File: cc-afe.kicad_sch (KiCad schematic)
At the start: 10 parts

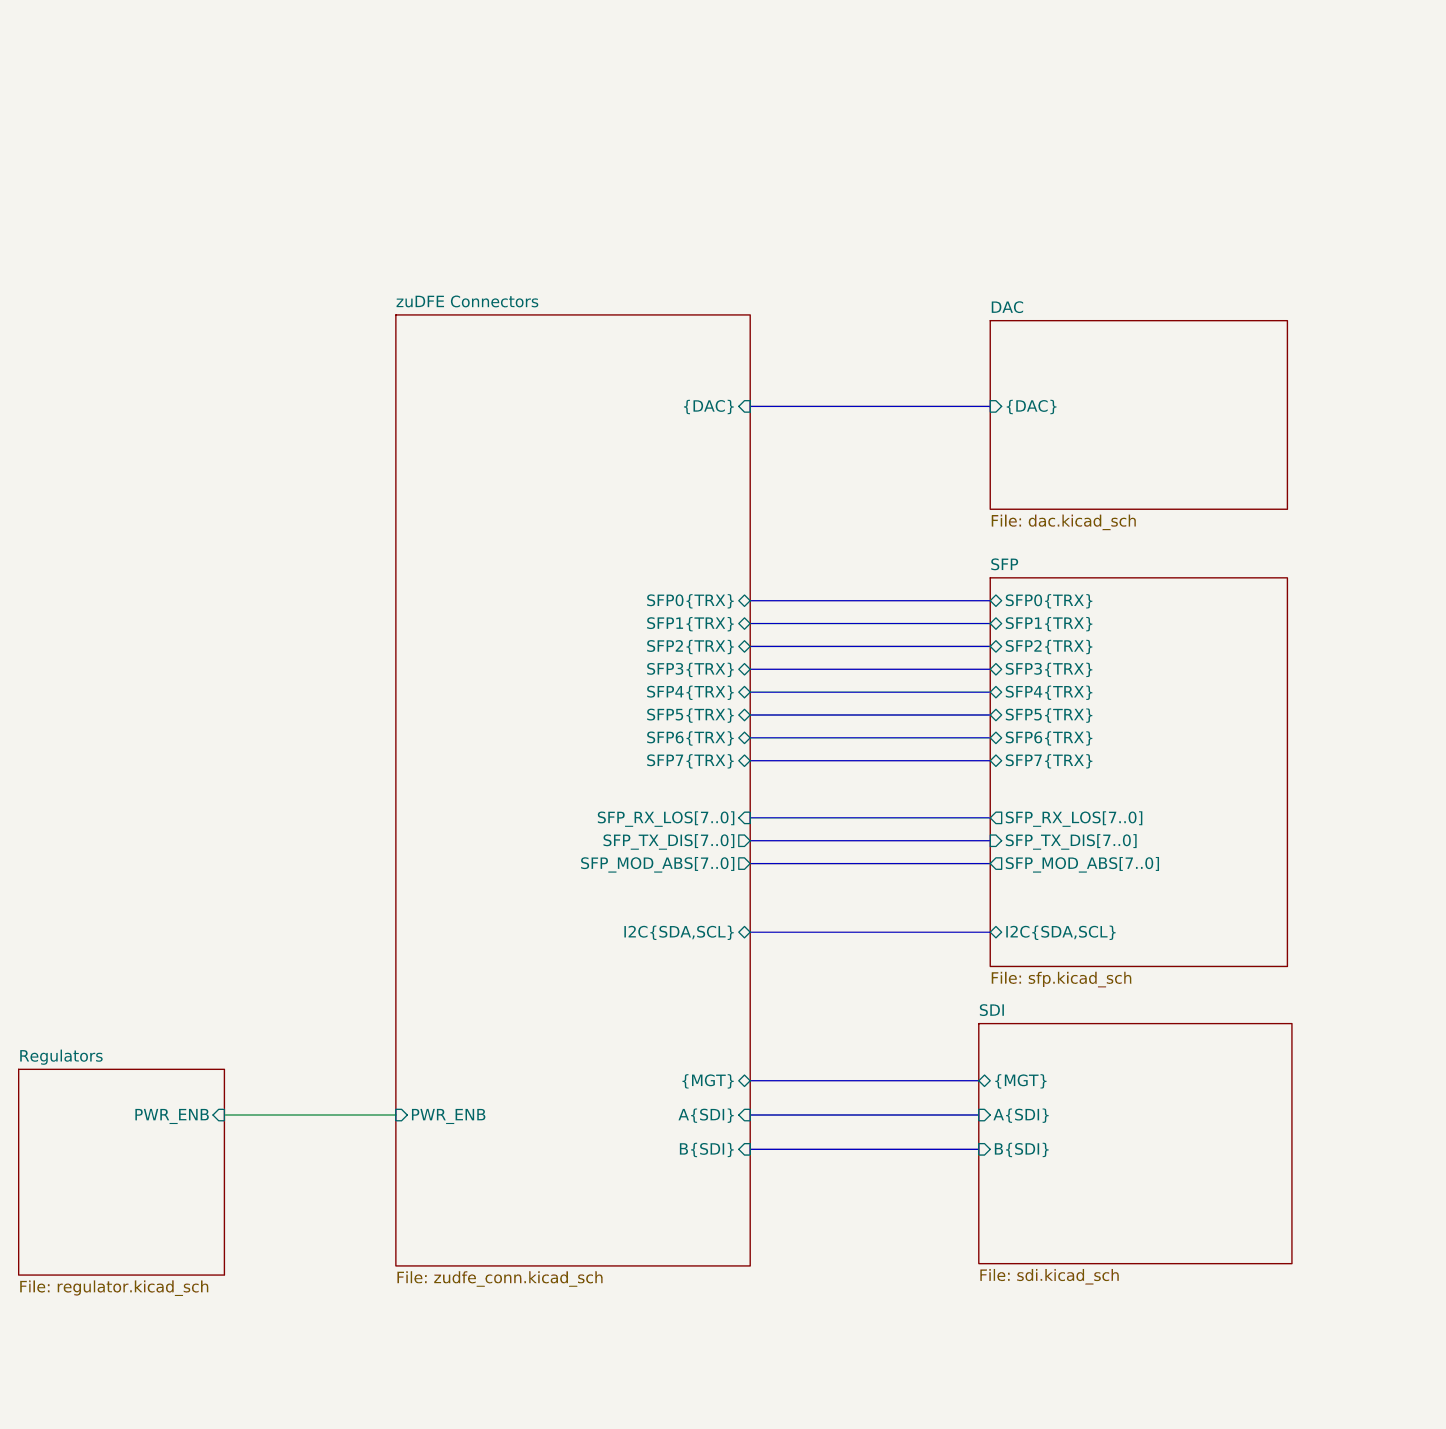
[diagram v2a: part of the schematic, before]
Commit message: Add digital Outputs
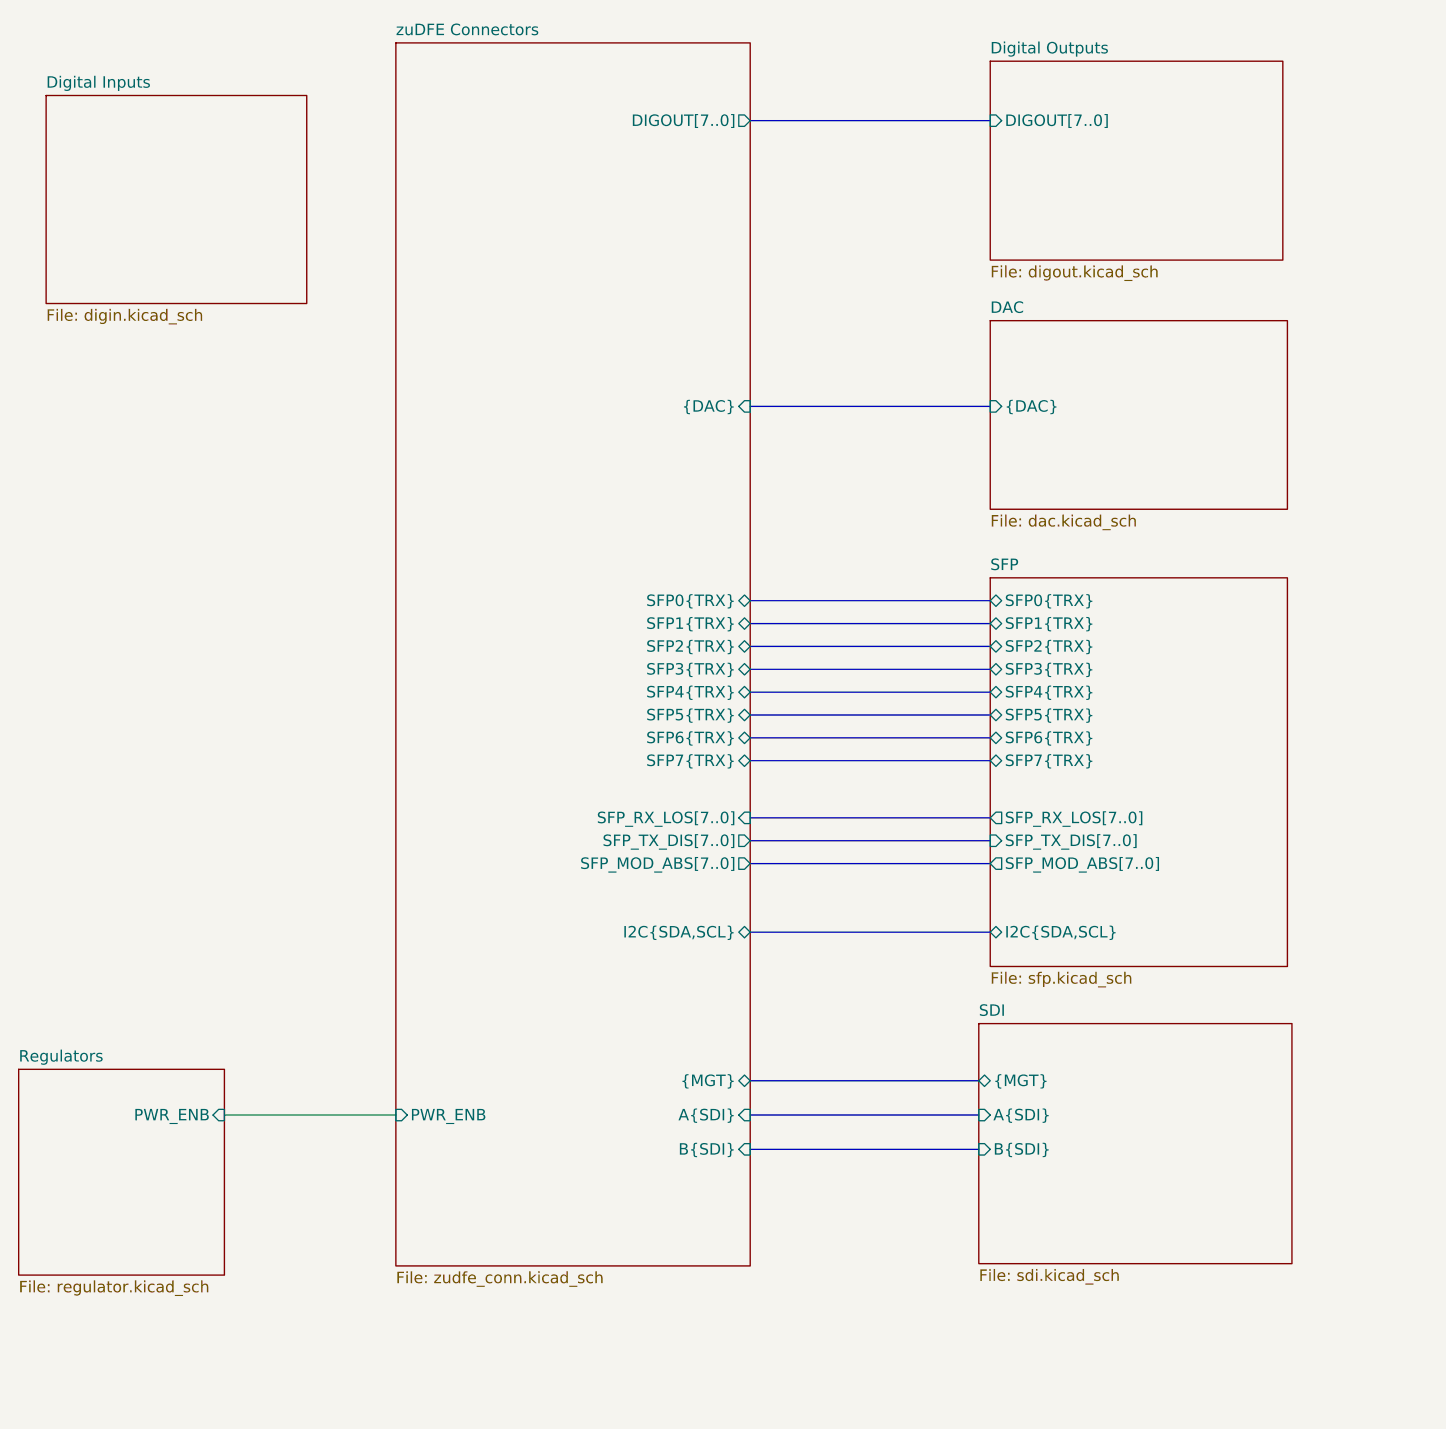
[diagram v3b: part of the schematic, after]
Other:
- added sheet Digital Inputs (digin.kicad_sch)
- added sheet Digital Outputs (digout.kicad_sch)
- sheet zuDFE Connectors ports: added DIGOUT[7..0]; removed none
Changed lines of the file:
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@@
+		)
+	)
+	(bus
+		(pts
+			(xy 214.63 48.26) (xy 241.3 48.26)
+		)
+		(stroke
+			(width 0)
+			(type default)
 		)
 	)
@@
 	)
 	(sheet
-		(at 175.26 69.85)
-		(size 39.37 105.664)
+		(at 175.26 39.624)
+		(size 39.37 135.89)
 		(exclude_from_sim no)
 		(in_bom yes)
@@
 		)
 		(property "Sheetname" "zuDFE Connectors"
-			(at 175.26 69.1384 0)
+			(at 175.26 38.9124 0)
 			(effects
 				(font
@@
 		(pin "{MGT}" bidirectional
 			(at 214.63 154.94 0)
+			(effects
+				(font
+					(size 1.27 1.27)
+				)
+				(justify right)
+			)
+		)
+		(pin "DIGOUT[7..0]" output
+			(at 214.63 48.26 0)
 			(effects
 				(font
@@
 				)
 			)
+		)
+	)
+	(sheet
+		(at 136.398 45.466)
+		(size 28.956 23.114)
+		(exclude_from_sim no)
+		(in_bom yes)
+		(on_board yes)
+		(dnp no)
+		(fields_autoplaced yes)
+		(stroke
+			(width 0.1524)
+			(type solid)
+		)
+		(fill
+			(color 255 255 194 1.0000)
+		)
+		(property "Sheetname" "Digital Inputs"
+			(at 136.398 44.7544 0)
+			(effects
+				(font
+					(size 1.27 1.27)
+				)
+				(justify left bottom)
+			)
+		)
+		(property "Sheetfile" "digin.kicad_sch"
+			(at 136.398 69.1646 0)
+			(effects
+				(font
+					(size 1.27 1.27)
+				)
+				(justify left top)
+			)
+		)
+		(instances
+			(project "cc-afe"
+				(path "/40891cc8-bf64-41f4-8f69-a607d7b280eb"
+					(page "8")
+				)
+			)
+		)
+	)
+	(sheet
+		(at 241.3 41.656)
+		(size 32.512 22.098)
+		(exclude_from_sim no)
+		(in_bom yes)
+		(on_board yes)
+		(dnp no)
+		(fields_autoplaced yes)
+		(stroke
+			(width 0.1524)
+			(type solid)
+		)
+		(fill
+			(color 255 255 194 1.0000)
+		)
+		(property "Sheetname" "Digital Outputs"
+			(at 241.3 40.9444 0)
+			(effects
+				(font
+					(size 1.27 1.27)
+				)
+				(justify left bottom)
+			)
+		)
+		(property "Sheetfile" "digout.kicad_sch"
+			(at 241.3 64.3386 0)
+			(effects
+				(font
+					(size 1.27 1.27)
+				)
+				(justify left top)
+			)
+		)
+		(pin "DIGOUT[7..0]" input
+			(at 241.3 48.26 180)
+			(effects
+				(font
+					(size 1.27 1.27)
+				)
+				(justify left)
+			)
+		)
+		(instances
+			(project "cc-afe"
+				(path "/40891cc8-bf64-41f4-8f69-a607d7b280eb"
+					(page "7")
+				)
+			)
